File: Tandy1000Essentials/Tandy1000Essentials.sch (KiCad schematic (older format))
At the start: 17 parts, among them J1 IDE_CONNECTOR, J2 CF Adapter Power, J3 Jumpers, J4 Bus_ISA_8bit, U1 BIOS FLASH, U2 74HCT245, U3 GAL22V10, U4 DS1315, U5 AS6C4008-55PCN, Y1 32.768 KHz

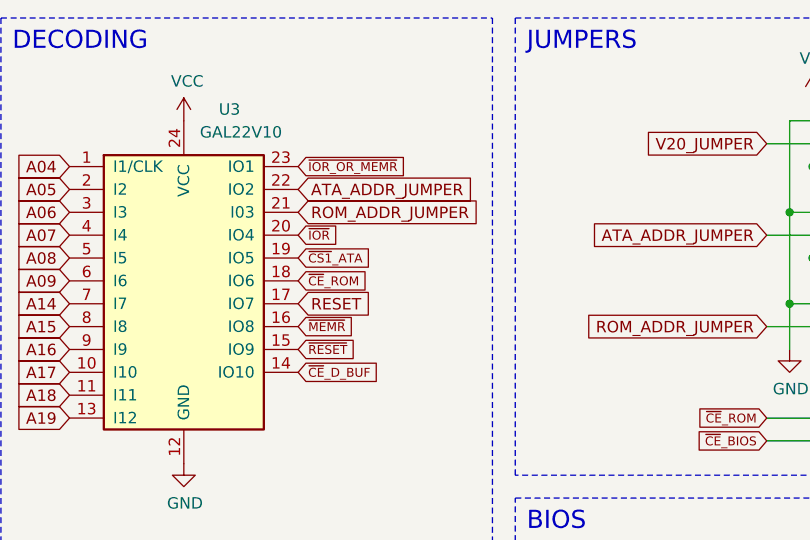
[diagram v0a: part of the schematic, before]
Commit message: Tandy1000Essentials: Layout passing DRC. Much cleanup still required.
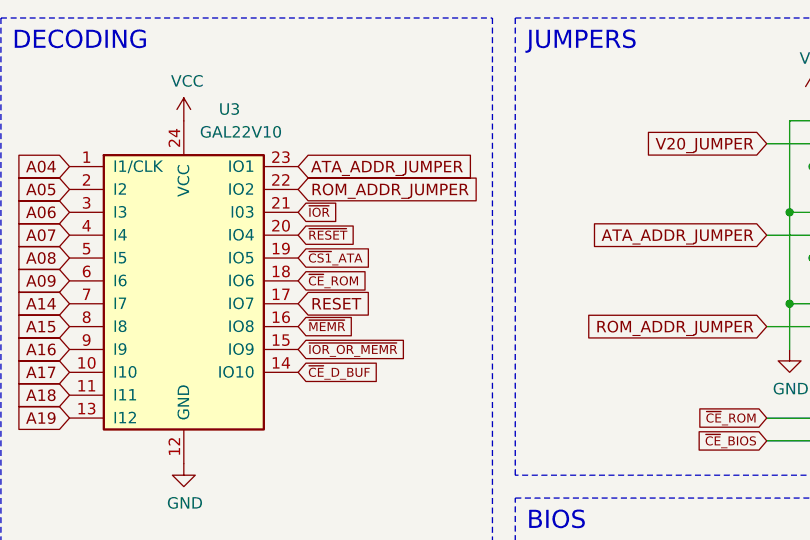
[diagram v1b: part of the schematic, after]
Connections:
- net ATA_ADDR_JUMPER: now also U3.23 (IO1); no longer U3.22 (IO2)
- net ROM_ADDR_JUMPER: now also U3.22 (IO2); no longer U3.21 (I03)
- net ~IOR: now also U3.21 (I03); no longer U3.20 (IO4)
- net ~IOR_OR_MEMR: now also U3.15 (IO9); no longer U3.23 (IO1)
- net ~RESET: now also U3.20 (IO4); no longer U3.15 (IO9)
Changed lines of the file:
@@
 Text GLabel 4950 1600 2    39   Input ~ 0
 ~CS1~_ATA
-Text GLabel 4950 2000 2    39   Input ~ 0
-~RESET
 Text GLabel 4950 1700 2    39   Input ~ 0
 ~CE~_ROM
@@
 NoConn ~ 1500 1600
 NoConn ~ 1500 1800
-Text GLabel 4950 1800 2    50   Input ~ 0
-RESET
 Wire Wire Line
 	9950 2750 10400 2750
@@
 Text GLabel 4150 4750 0    39   Input ~ 0
 ~IOR_OR_MEMR
-Text GLabel 4950 1400 2    50   Input ~ 0
+Text GLabel 4950 1300 2    50   Input ~ 0
 ROM_ADDR_JUMPER
-Text GLabel 4950 1300 2    50   Input ~ 0
+Text GLabel 4950 1200 2    50   Input ~ 0
 ATA_ADDR_JUMPER
 $Comp
@@
 Text GLabel 3950 1800 0    50   Input ~ 0
 A14
-Text GLabel 4950 1200 2    39   Input ~ 0
-~IOR_OR_MEMR
-Text GLabel 4950 1500 2    39   Input ~ 0
-~IOR
 Text GLabel 4950 1900 2    39   Input ~ 0
 ~MEMR
@@
 	1    0    0    -1
 $EndComp
+Text GLabel 4950 2000 2    39   Input ~ 0
+~IOR_OR_MEMR
+Text GLabel 4950 1800 2    50   Input ~ 0
+RESET
+Text GLabel 4950 1500 2    39   Input ~ 0
+~RESET
+Text GLabel 4950 1400 2    39   Input ~ 0
+~IOR
 $EndSCHEMATC

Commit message: Tandy1000Essentials: More refinement of layout, fix ERC error due to incorrect 22V10 pinout.
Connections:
- net ~CE~_BIOS: now also J3.11 (Pin_11); no longer J3.12 (Pin_12), U4.11 (~CEI)
- net ~CE~_BIOS_THRU: now reaches J3.10 (Pin_10)
- net ~CE~_BIOS_THRU: now also U4.10 (~CEO)
- removed net ~CE~_ROM: J3.11 (Pin_11), U3.18 (IO6), U4.10 (~CEO)
- new net ~CE~_BIOS_DECODE: J3.12 (Pin_12), U3.18 (IO6), U4.11 (~CEI)
- no-connect marks 40 -> 39
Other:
- moved on the sheet: U1
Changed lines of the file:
@@
 L Memory_Flash:SST39SF040 U1
 U 1 1 603B5177
-P 7300 4400
-F 0 "U1" H 7300 5971 50  0000 C CNN
-F 1 "BIOS FLASH" H 7300 5880 50  0000 C CNN
-F 2 "Package_DIP:DIP-32_W15.24mm_Socket" H 7300 4700 50  0001 C CNN
-F 3 "http://ww1.microchip.com/downloads/en/DeviceDoc/25022B.pdf" H 7300 4700 50  0001 C CNN
-F 4 "SST39SF010, SST39SF020, SST39SF040 or similar" H 7300 5789 50  0000 C CNN "Note"
-	1    7300 4400
+P 7300 4800
+F 0 "U1" H 7300 6371 50  0000 C CNN
+F 1 "BIOS FLASH" H 7300 6280 50  0000 C CNN
+F 2 "Package_DIP:DIP-32_W15.24mm_Socket" H 7300 5100 50  0001 C CNN
+F 3 "http://ww1.microchip.com/downloads/en/DeviceDoc/25022B.pdf" H 7300 5100 50  0001 C CNN
+F 4 "SST39SF010, SST39SF020, SST39SF040 or similar" H 7300 6189 50  0000 C CNN "Note"
+	1    7300 4800
 	1    0    0    -1
 $EndComp
@@
 	1    0    0    -1
 $EndComp
-Text GLabel 6700 3200 0    50   Input ~ 0
+Text GLabel 6700 3600 0    50   Input ~ 0
 A00
-Text GLabel 6700 3300 0    50   Input ~ 0
+Text GLabel 6700 3700 0    50   Input ~ 0
 A01
-Text GLabel 6700 3400 0    50   Input ~ 0
+Text GLabel 6700 3800 0    50   Input ~ 0
 A02
-Text GLabel 6700 3500 0    50   Input ~ 0
+Text GLabel 6700 3900 0    50   Input ~ 0
 A03
-Text GLabel 6700 3600 0    50   Input ~ 0
+Text GLabel 6700 4000 0    50   Input ~ 0
 A04
-Text GLabel 6700 3700 0    50   Input ~ 0
+Text GLabel 6700 4100 0    50   Input ~ 0
 A05
-Text GLabel 6700 3800 0    50   Input ~ 0
+Text GLabel 6700 4200 0    50   Input ~ 0
 A06
-Text GLabel 6700 3900 0    50   Input ~ 0
+Text GLabel 6700 4300 0    50   Input ~ 0
 A07
-Text GLabel 6700 4000 0    50   Input ~ 0
+Text GLabel 6700 4400 0    50   Input ~ 0
 A08
-Text GLabel 6700 4100 0    50   Input ~ 0
+Text GLabel 6700 4500 0    50   Input ~ 0
 A09
-Text GLabel 6700 4200 0    50   Input ~ 0
+Text GLabel 6700 4600 0    50   Input ~ 0
 A10
-Text GLabel 6700 4300 0    50   Input ~ 0
+Text GLabel 6700 4700 0    50   Input ~ 0
 A11
-Text GLabel 6700 4400 0    50   Input ~ 0
+Text GLabel 6700 4800 0    50   Input ~ 0
 A12
-Text GLabel 6700 4500 0    50   Input ~ 0
+Text GLabel 6700 4900 0    50   Input ~ 0
 A13
 Wire Wire Line
-	6700 5000 6300 5000
-Wire Wire Line
-	6300 5000 6300 5700
+	6700 5400 6300 5400
+Wire Wire Line
+	6300 5400 6300 6100
 $Comp
 L power:GND #PWR0112
 U 1 1 6042FC5C
-P 6300 5700
-F 0 "#PWR0112" H 6300 5450 50  0001 C CNN
-F 1 "GND" H 6305 5527 50  0000 C CNN
-F 2 "" H 6300 5700 50  0001 C CNN
-F 3 "" H 6300 5700 50  0001 C CNN
-	1    6300 5700
-	1    0    0    -1
-$EndComp
-Text GLabel 6700 5200 0    39   Input ~ 0
+P 6300 6100
+F 0 "#PWR0112" H 6300 5850 50  0001 C CNN
+F 1 "GND" H 6305 5927 50  0000 C CNN
+F 2 "" H 6300 6100 50  0001 C CNN
+F 3 "" H 6300 6100 50  0001 C CNN
+	1    6300 6100
+	1    0    0    -1
+$EndComp
+Text GLabel 6700 5600 0    39   Input ~ 0
 ~MEMW
-Text GLabel 6700 5500 0    39   Input ~ 0
+Text GLabel 6700 5900 0    39   Input ~ 0
 ~MEMR
-Text GLabel 6700 5400 0    39   Input ~ 0
+Text GLabel 6700 5800 0    39   Input ~ 0
 ~CE~_BIOS
-Text GLabel 7900 3200 2    50   Input ~ 0
+Text GLabel 7900 3600 2    50   Input ~ 0
 D0_BUF
-Text GLabel 7900 3300 2    50   Input ~ 0
+Text GLabel 7900 3700 2    50   Input ~ 0
 D1_BUF
-Text GLabel 7900 3400 2    50   Input ~ 0
+Text GLabel 7900 3800 2    50   Input ~ 0
 D2_BUF
-Text GLabel 7900 3500 2    50   Input ~ 0
+Text GLabel 7900 3900 2    50   Input ~ 0
 D3_BUF
-Text GLabel 7900 3600 2    50   Input ~ 0
+Text GLabel 7900 4000 2    50   Input ~ 0
 D4_BUF
-Text GLabel 7900 3700 2    50   Input ~ 0
+Text GLabel 7900 4100 2    50   Input ~ 0
 D5_BUF
-Text GLabel 7900 3800 2    50   Input ~ 0
+Text GLabel 7900 4200 2    50   Input ~ 0
 D6_BUF
-Text GLabel 7900 3900 2    50   Input ~ 0
+Text GLabel 7900 4300 2    50   Input ~ 0
 D7_BUF
 Text GLabel 4950 1600 2    39   Input ~ 0
 ~CS1~_ATA
 Text GLabel 4950 1700 2    39   Input ~ 0
-~CE~_ROM
+~CE~_BIOS_DECODE
 Text GLabel 4950 2100 2    39   Input ~ 0
 ~CE~_D_BUF
@@
 Text GLabel 3950 1900 0    50   Input ~ 0
 A15
-Text GLabel 6700 4700 0    50   Input ~ 0
+Text GLabel 6700 5100 0    50   Input ~ 0
 V20_JUMPER
 Wire Wire Line
-	6700 4800 6300 4800
-Wire Wire Line
-	6300 4800 6300 4900
-Connection ~ 6300 5000
-Wire Wire Line
-	6700 4900 6300 4900
-Connection ~ 6300 4900
-Wire Wire Line
-	6300 4900 6300 5000
-Text GLabel 6700 4600 0    50   Input ~ 0
+	6700 5200 6300 5200
+Wire Wire Line
+	6300 5200 6300 5300
+Connection ~ 6300 5400
+Wire Wire Line
+	6700 5300 6300 5300
+Connection ~ 6300 5300
+Wire Wire Line
+	6300 5300 6300 5400
+Text GLabel 6700 5000 0    50   Input ~ 0
 ATA_ADDR_JUMPER
 $Comp
@@
 Text Notes 3700 700  0    79   ~ 0
 DECODING
-Text Notes 5950 2800 0    79   ~ 0
+Text Notes 5950 3200 0    79   ~ 0
 BIOS
 Text Notes 8500 700  0    79   ~ 0
@@
 	3650 550  3650 2900
 Wire Notes Line
-	8350 2650 8350 6450
-Wire Notes Line
-	8350 6450 5900 6450
-Wire Notes Line
-	5900 2550 5900 550
-Wire Notes Line
-	8350 2550 5900 2550
-Wire Notes Line
-	8350 550  8350 2550
+	8350 2950 5900 2950
 Wire Notes Line
 	5900 550  8350 550
@@
 L power:GND #PWR0104
 U 1 1 6067888C
-P 7100 2000
-F 0 "#PWR0104" H 7100 1750 50  0001 C CNN
-F 1 "GND" H 7105 1827 50  0000 C CNN
-F 2 "" H 7100 2000 50  0001 C CNN
-F 3 "" H 7100 2000 50  0001 C CNN
-	1    7100 2000
+P 7100 2600
+F 0 "#PWR0104" H 7100 2350 50  0001 C CNN
+F 1 "GND" H 7105 2427 50  0000 C CNN
+F 2 "" H 7100 2600 50  0001 C CNN
+F 3 "" H 7100 2600 50  0001 C CNN
+	1    7100 2600
 	1    0    0    -1
 $EndComp
@@
 	1    0    0    -1
 $EndComp
-NoConn ~ 7300 2200
 $Comp
 L 00Common:Bus_ISA_8bit J4
@@
 	1    0    0    -1
 $EndComp
+Text GLabel 7000 2400 0    39   Input ~ 0
+~CE~_BIOS_DECODE
 Text GLabel 7000 2300 0    39   Input ~ 0
-~CE~_ROM
-Text GLabel 7000 2400 0    39   Input ~ 0
 ~CE~_BIOS
 Wire Wire Line
@@
 $EndComp
 Wire Wire Line
-	7100 1800 7100 2000
+	7100 1800 7100 2600
 Wire Wire Line
 	7200 1600 7200 2000
@@
 Wire Wire Line
 	3800 6700 4100 6700
+Text GLabel 4100 6800 2    39   Input ~ 0
+~CE~_BIOS_THRU
+Wire Wire Line
+	3800 6800 4100 6800
 Text GLabel 4100 6700 2    39   Input ~ 0
-~CE~_BIOS
-Wire Wire Line
-	3800 6800 4100 6800
-Text GLabel 4100 6800 2    39   Input ~ 0
-~CE~_ROM
+~CE~_BIOS_DECODE
 Wire Wire Line
 	3800 6600 4100 6600
@@
 $EndComp
 Wire Notes Line
-	5900 6450 5900 2650
-Wire Notes Line
-	5900 2650 8350 2650
+	5900 3050 8350 3050
 Wire Notes Line
 	5800 550  5800 2900
@@
 Text GLabel 4950 1400 2    39   Input ~ 0
 ~IOR
+Wire Notes Line
+	5900 2950 5900 550
+Wire Notes Line
+	8350 550  8350 2950
+Wire Notes Line
+	5900 6450 5900 3050
+Wire Notes Line
+	8350 6450 5900 6450
+Wire Notes Line
+	8350 3050 8350 6450
+Text GLabel 7000 2200 0    39   Input ~ 0
+~CE~_BIOS_THRU
+Wire Wire Line
+	7000 2200 7300 2200
 $EndSCHEMATC

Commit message: Fix location of CF adapter power for all boards that use it. Also the mounting holes in the schematic for the same boards. Finishing touches to Tandy 1000 Essentials.
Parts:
- added H1, H2, H3, H4: MountingHole_Pad, MountingHole:MountingHole_3.5mm_Pad, symbol Mechanical:MountingHole_Pad
- J2: footprint Connector_PinHeader_2.54mm:PinHeader_1x02_P2.54mm_Vertical -> Connector_PinSocket_2.54mm:PinSocket_1x01_P2.54mm_Vertical; symbol Connector_Generic:Conn_01x02 -> Connector_Generic:Conn_01x01
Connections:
- net GND: now also H1.1, H2.1, H3.1, H4.1; no longer J2.2 (Pin_2)
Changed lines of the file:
@@
 $EndComp
 $Comp
-L Connector_Generic:Conn_01x02 J2
+L Connector_Generic:Conn_01x01 J2
 U 1 1 603E8D26
-P 10850 1200
-F 0 "J2" H 10800 1350 50  0000 L CNN
-F 1 "CF Adapter Power" V 11000 800 50  0000 L CNN
-F 2 "Connector_PinHeader_2.54mm:PinHeader_1x02_P2.54mm_Vertical" H 10850 1200 50  0001 C CNN
-F 3 "~" H 10850 1200 50  0001 C CNN
-	1    10850 1200
+P 10750 950
+F 0 "J2" H 10700 1100 50  0000 L CNN
+F 1 "CF Adapter Power" V 10900 550 50  0000 L CNN
+F 2 "Connector_PinSocket_2.54mm:PinSocket_1x01_P2.54mm_Vertical" H 10750 950 50  0001 C CNN
+F 3 "~" H 10750 950 50  0001 C CNN
+	1    10750 950
 	1    0    0    -1
 $EndComp
@@
 L power:GND #PWR0123
 U 1 1 603E9698
-P 10650 1300
-F 0 "#PWR0123" H 10650 1050 50  0001 C CNN
-F 1 "GND" H 10655 1127 50  0000 C CNN
-F 2 "" H 10650 1300 50  0001 C CNN
-F 3 "" H 10650 1300 50  0001 C CNN
-	1    10650 1300
+P 10500 2200
+F 0 "#PWR0123" H 10500 1950 50  0001 C CNN
+F 1 "GND" H 10505 2027 50  0000 C CNN
+F 2 "" H 10500 2200 50  0001 C CNN
+F 3 "" H 10500 2200 50  0001 C CNN
+	1    10500 2200
 	1    0    0    -1
 $EndComp
@@
 L power:VCC #PWR0124
 U 1 1 603E9A78
-P 10650 1200
-F 0 "#PWR0124" H 10650 1050 50  0001 C CNN
-F 1 "VCC" H 10665 1373 50  0000 C CNN
-F 2 "" H 10650 1200 50  0001 C CNN
-F 3 "" H 10650 1200 50  0001 C CNN
-	1    10650 1200
+P 10550 950
+F 0 "#PWR0124" H 10550 800 50  0001 C CNN
+F 1 "VCC" H 10565 1123 50  0000 C CNN
+F 2 "" H 10550 950 50  0001 C CNN
+F 3 "" H 10550 950 50  0001 C CNN
+	1    10550 950
 	1    0    0    -1
 $EndComp
@@
 Wire Wire Line
 	7000 2200 7300 2200
+$Comp
+L Mechanical:MountingHole_Pad H1
+U 1 1 60909CFD
+P 10700 1500
+F 0 "H1" V 10700 1650 50  0000 L CNN
+F 1 "MountingHole_Pad" V 10745 1650 50  0001 L CNN
+F 2 "MountingHole:MountingHole_3.5mm_Pad" H 10700 1500 50  0001 C CNN
+F 3 "~" H 10700 1500 50  0001 C CNN
+	1    10700 1500
+	0    1    1    0
+$EndComp
+$Comp
+L Mechanical:MountingHole_Pad H2
+U 1 1 6090B119
+P 10700 1700
+F 0 "H2" V 10700 1850 50  0000 L CNN
+F 1 "MountingHole_Pad" V 10745 1850 50  0001 L CNN
+F 2 "MountingHole:MountingHole_3.5mm_Pad" H 10700 1700 50  0001 C CNN
+F 3 "~" H 10700 1700 50  0001 C CNN
+	1    10700 1700
+	0    1    1    0
+$EndComp
+$Comp
+L Mechanical:MountingHole_Pad H3
+U 1 1 6090B31B
+P 10700 1900
+F 0 "H3" V 10700 2050 50  0000 L CNN
+F 1 "MountingHole_Pad" V 10745 2050 50  0001 L CNN
+F 2 "MountingHole:MountingHole_3.5mm_Pad" H 10700 1900 50  0001 C CNN
+F 3 "~" H 10700 1900 50  0001 C CNN
+	1    10700 1900
+	0    1    1    0
+$EndComp
+$Comp
+L Mechanical:MountingHole_Pad H4
+U 1 1 6090B462
+P 10700 2100
+F 0 "H4" V 10700 2250 50  0000 L CNN
+F 1 "MountingHole_Pad" V 10745 2250 50  0001 L CNN
+F 2 "MountingHole:MountingHole_3.5mm_Pad" H 10700 2100 50  0001 C CNN
+F 3 "~" H 10700 2100 50  0001 C CNN
+	1    10700 2100
+	0    1    1    0
+$EndComp
+Wire Wire Line
+	10600 1500 10500 1500
+Wire Wire Line
+	10500 1500 10500 1700
+Wire Wire Line
+	10500 2100 10600 2100
+Connection ~ 10500 2100
+Wire Wire Line
+	10500 2100 10500 2200
+Wire Wire Line
+	10600 1900 10500 1900
+Connection ~ 10500 1900
+Wire Wire Line
+	10500 1900 10500 2100
+Wire Wire Line
+	10500 1700 10600 1700
+Connection ~ 10500 1700
+Wire Wire Line
+	10500 1700 10500 1900
 $EndSCHEMATC

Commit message: Tandy1000Essentials: Add programmable logic. Also schematic / board fixes that became apparent when writing the logic equations.
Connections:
- net A14: no longer U3.7 (I7)
- net GND: now also U2.19 (CE)
- net RESET: now also U3.7 (I7); no longer U3.17 (IO7)
- net ~IOR: no longer J1.25 (~IOR)
- net ~MEMR: now also U3.17 (IO7); no longer U1.24 (OE), U3.16 (IO8), U4.12 (~OE), U5.24 (OE#)
- net ~CE~_D_BUF renamed ~IOR~_DELAYED
- net ~IOR~_DELAYED: now also J1.25 (~IOR); no longer U2.19 (CE)
- new net ~MEMR~_DELAYED: U1.24 (OE), U3.16 (IO8), U4.12 (~OE), U5.24 (OE#)
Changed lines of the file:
@@
 L power:GND #PWR0107
 U 1 1 603E741A
-P 8650 3000
-F 0 "#PWR0107" H 8650 2750 50  0001 C CNN
-F 1 "GND" H 8655 2827 50  0000 C CNN
-F 2 "" H 8650 3000 50  0001 C CNN
-F 3 "" H 8650 3000 50  0001 C CNN
-	1    8650 3000
-	1    0    0    -1
-$EndComp
-Wire Wire Line
-	8650 3000 8650 1850
-Wire Wire Line
-	8650 1850 9150 1850
+P 8550 3000
+F 0 "#PWR0107" H 8550 2750 50  0001 C CNN
+F 1 "GND" H 8555 2827 50  0000 C CNN
+F 2 "" H 8550 3000 50  0001 C CNN
+F 3 "" H 8550 3000 50  0001 C CNN
+	1    8550 3000
+	1    0    0    -1
+$EndComp
+Wire Wire Line
+	8550 3000 8550 1850
+Wire Wire Line
+	8550 1850 9150 1850
 Text GLabel 9150 2150 0    39   Input ~ 0
-~IOR
+~IOR~_DELAYED
 Text GLabel 9150 2050 0    39   Input ~ 0
 ~IOW
@@
 A13
 Wire Wire Line
-	6700 5400 6300 5400
-Wire Wire Line
-	6300 5400 6300 6100
+	6700 5400 6100 5400
+Wire Wire Line
+	6100 5400 6100 6100
 $Comp
 L power:GND #PWR0112
 U 1 1 6042FC5C
-P 6300 6100
-F 0 "#PWR0112" H 6300 5850 50  0001 C CNN
-F 1 "GND" H 6305 5927 50  0000 C CNN
-F 2 "" H 6300 6100 50  0001 C CNN
-F 3 "" H 6300 6100 50  0001 C CNN
-	1    6300 6100
+P 6100 6100
+F 0 "#PWR0112" H 6100 5850 50  0001 C CNN
+F 1 "GND" H 6105 5927 50  0000 C CNN
+F 2 "" H 6100 6100 50  0001 C CNN
+F 3 "" H 6100 6100 50  0001 C CNN
+	1    6100 6100
 	1    0    0    -1
 $EndComp
@@
 ~MEMW
 Text GLabel 6700 5900 0    39   Input ~ 0
-~MEMR
+~MEMR~_DELAYED
 Text GLabel 6700 5800 0    39   Input ~ 0
 ~CE~_BIOS
@@
 ~CE~_BIOS_DECODE
 Text GLabel 4950 2100 2    39   Input ~ 0
-~CE~_D_BUF
+~IOR~_DELAYED
 Text GLabel 2600 3400 2    50   Input ~ 0
 A06
@@
 V20_JUMPER
 Wire Wire Line
-	6700 5200 6300 5200
-Wire Wire Line
-	6300 5200 6300 5300
-Connection ~ 6300 5400
-Wire Wire Line
-	6700 5300 6300 5300
-Connection ~ 6300 5300
-Wire Wire Line
-	6300 5300 6300 5400
+	6700 5200 6100 5200
+Wire Wire Line
+	6100 5200 6100 5300
+Connection ~ 6100 5400
+Wire Wire Line
+	6700 5300 6100 5300
+Connection ~ 6100 5300
+Wire Wire Line
+	6100 5300 6100 5400
 Text GLabel 6700 5000 0    50   Input ~ 0
 ATA_ADDR_JUMPER
@@
 L power:VCC #PWR0125
 U 1 1 603F3CE5
-P 8850 2150
-F 0 "#PWR0125" H 8850 2000 50  0001 C CNN
-F 1 "VCC" H 8865 2323 50  0000 C CNN
-F 2 "" H 8850 2150 50  0001 C CNN
-F 3 "" H 8850 2150 50  0001 C CNN
-	1    8850 2150
-	1    0    0    -1
-$EndComp
-Wire Wire Line
-	9150 2350 8850 2350
-Wire Wire Line
-	8850 2350 8850 2150
+P 8650 2150
+F 0 "#PWR0125" H 8650 2000 50  0001 C CNN
+F 1 "VCC" H 8665 2323 50  0000 C CNN
+F 2 "" H 8650 2150 50  0001 C CNN
+F 3 "" H 8650 2150 50  0001 C CNN
+	1    8650 2150
+	1    0    0    -1
+$EndComp
+Wire Wire Line
+	9150 2350 8650 2350
+Wire Wire Line
+	8650 2350 8650 2150
 Wire Wire Line
 	10300 2150 10300 2350
@@
 Text GLabel 9150 2750 0    39   Input ~ 0
 ~CS1~_ATA
-Text GLabel 4150 4850 0    39   Input ~ 0
-~CE~_D_BUF
 $Comp
 L power:GND #PWR0109
@@
 	2500 2600 2600 2600
 Text GLabel 3950 1800 0    50   Input ~ 0
-A14
-Text GLabel 4950 1900 2    39   Input ~ 0
+RESET
+Text GLabel 4950 1800 2    39   Input ~ 0
 ~MEMR
 $Comp
@@
 	3800 6600 4100 6600
 Text GLabel 4100 6600 2    39   Input ~ 0
-~MEMR
+~MEMR~_DELAYED
 $Comp
 L power:GND #PWR0127
@@
 A19
 Text GLabel 10200 5200 2    39   Input ~ 0
-~MEMR
+~MEMR~_DELAYED
 Text GLabel 10200 5300 2    39   Input ~ 0
 ~MEMW
@@
 Text GLabel 4950 2000 2    39   Input ~ 0
 ~IOR_OR_MEMR
-Text GLabel 4950 1800 2    50   Input ~ 0
-RESET
 Text GLabel 4950 1500 2    39   Input ~ 0
 ~RESET
@@
 Wire Wire Line
 	10500 1700 10500 1900
+Text GLabel 4950 1900 2    39   Input ~ 0
+~MEMR~_DELAYED
+$Comp
+L power:GND #PWR0134
+U 1 1 60C19D5B
+P 4050 5150
+F 0 "#PWR0134" H 4050 4900 50  0001 C CNN
+F 1 "GND" H 4055 4977 50  0000 C CNN
+F 2 "" H 4050 5150 50  0001 C CNN
+F 3 "" H 4050 5150 50  0001 C CNN
+	1    4050 5150
+	1    0    0    -1
+$EndComp
+Wire Wire Line
+	4150 4850 4050 4850
+Wire Wire Line
+	4050 4850 4050 5150
 $EndSCHEMATC
